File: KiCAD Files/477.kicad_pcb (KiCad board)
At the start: 2 copper layers, 101.7 x 59.6 mm, 74 parts, among them IC1 W25N01GVSFIG, IC2 W25N01GVSFIG, IC3 W25N01GVSFIG, IC4 W25N01GVSFIG, IC5 AZ1117IH-3.3TRG1, IC6 USBLC6-2SC6, J1 BM06B-SRSS-TBT_LF__SN_, J2 6364372-2, J3 TSW-103-14-S-D, J4 TSW-103-14-S-D, J5 BM07B-SRSS-TB_LF__SN_, J6 BM09B-SRSS-TB_LF__SN_, J7 TSW-105-05-F-S, U1 STM32H7A3RGTx, Y1 ABM8G-48.000MHZ-18-D2Y-T

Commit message: fixed weird routing
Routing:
- net VBAT: track 417.9 -> 404.6 mm
- net +5V: track 175.4 -> 163.6 mm

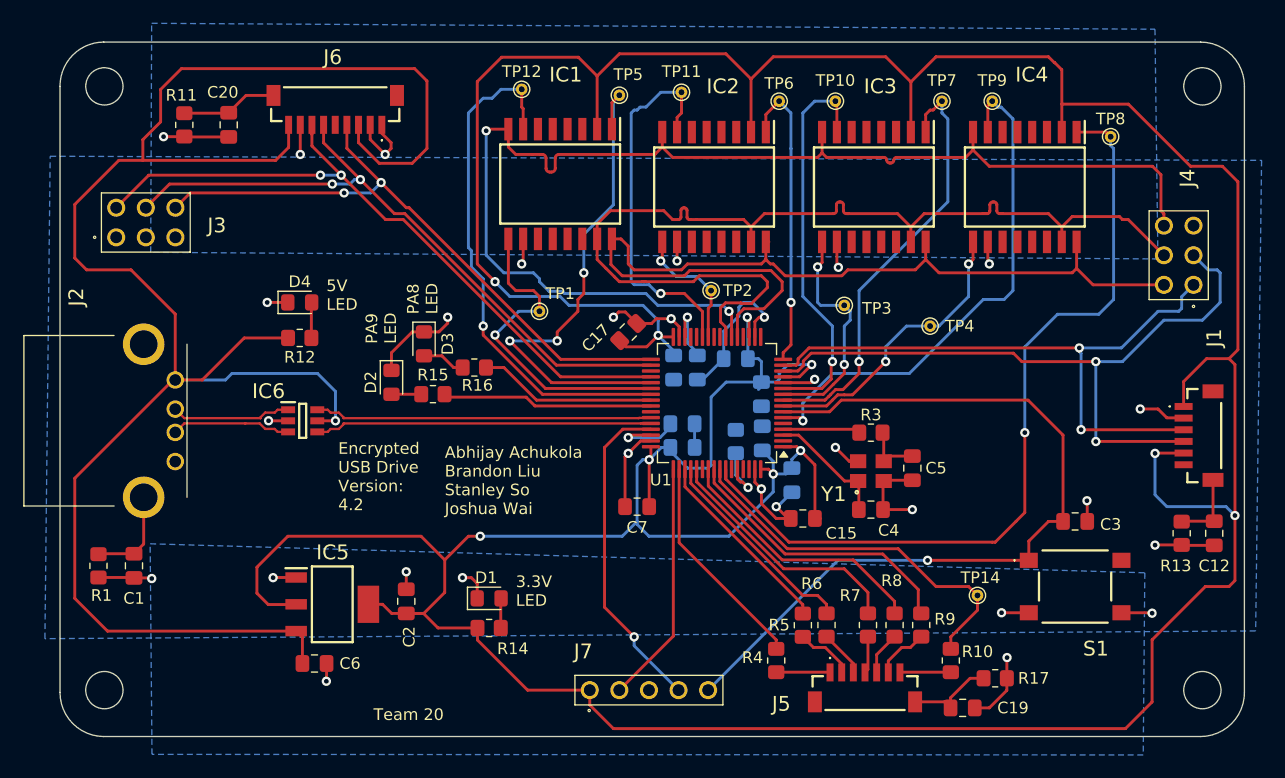
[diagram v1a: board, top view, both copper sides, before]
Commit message: made VBAT pad bigger
hi Joshua
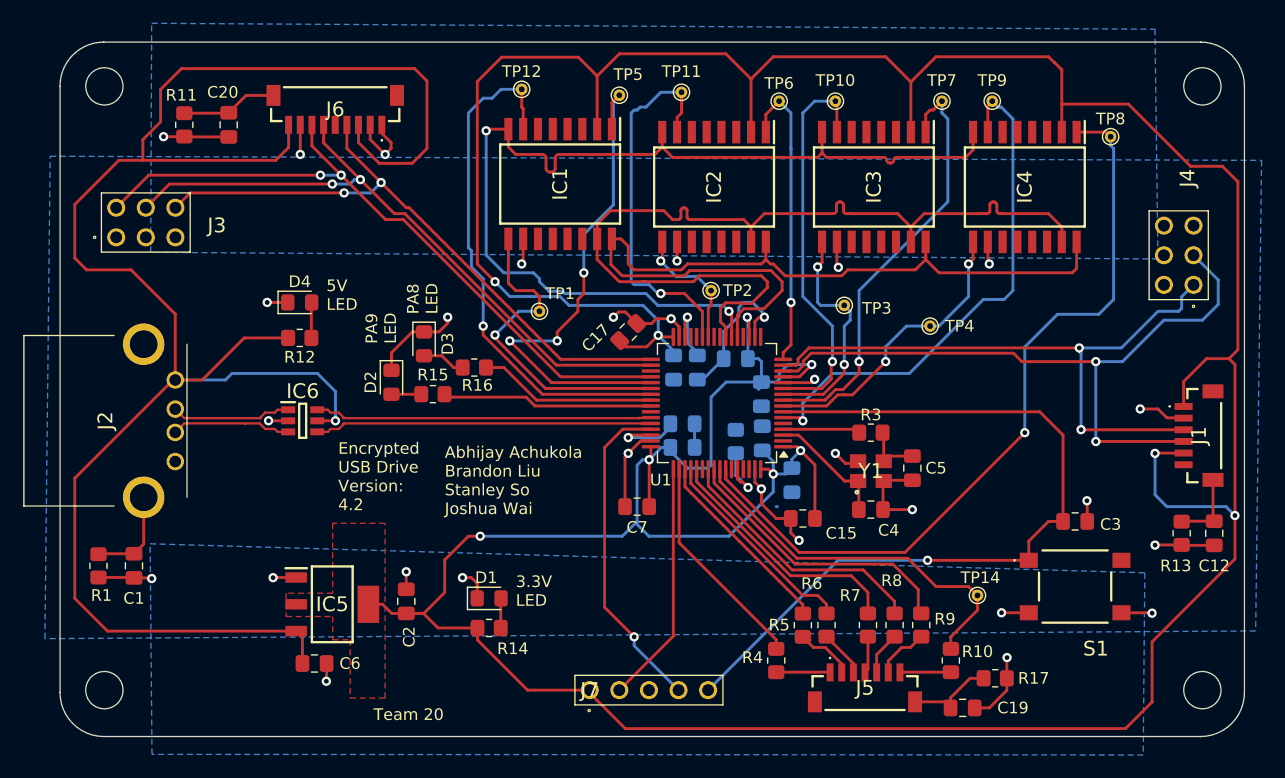
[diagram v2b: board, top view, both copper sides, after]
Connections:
- J4 pad 2: PA5/SCK -> unconnected-(J4-Pad2)
- J4 pad 4: PA7/MOSI -> unconnected-(J4-Pad4)
- J4 pad 6: PA6/MISO -> unconnected-(J4-Pad6)
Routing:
- net VBAT: track 404.6 -> 378.8 mm
- net PA6/MISO: track 109.8 -> 88.3 mm
- net PA7/MOSI: track 88.7 -> 78.2 mm
- net PA5/SCK: track 83.6 -> 74.8 mm
- net PB6/HOLD4: track 70.5 -> 67.2 mm
- net GND: track 120.9 -> 120.1 mm
- net nRST: track 71.3 -> 70.5 mm
- net unconnected-(J4-Pad2): track 0.00 -> 0.70 mm
- net PA0/FP TX: track 60.6 -> 60.0 mm
- added copper zone on F.Cu, net VBAT

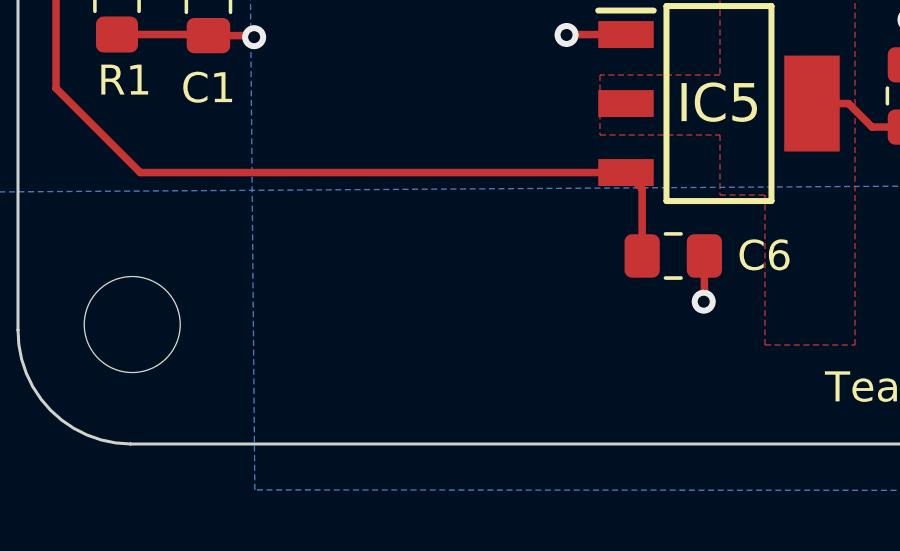
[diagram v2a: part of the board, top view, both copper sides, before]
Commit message: added big ground pad that we can clip oscilloscope to
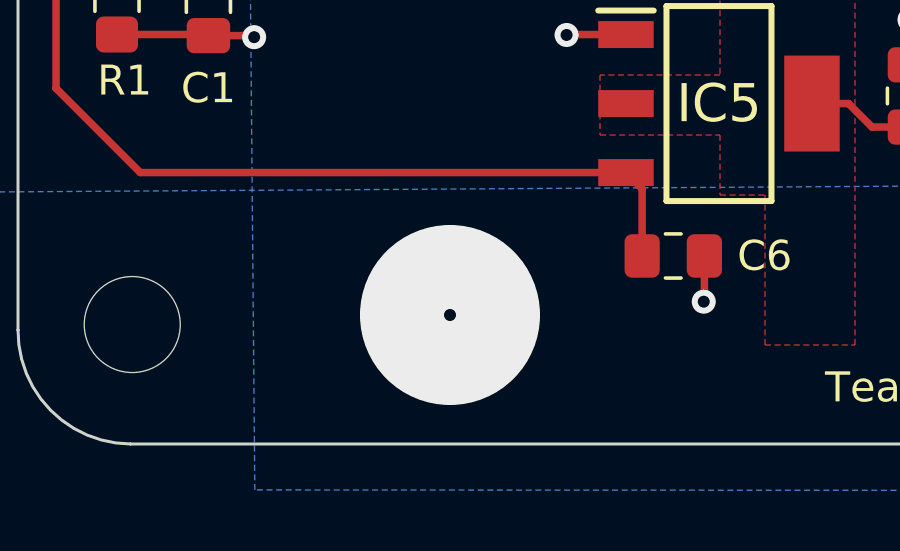
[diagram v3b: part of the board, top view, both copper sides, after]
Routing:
- net GND: vias 30 -> 31
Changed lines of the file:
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@@
+	)
+	(via
+		(at 100 131)
+		(size 6)
+		(drill 0.4)
+		(layers "F.Cu" "B.Cu")
+		(free yes)
+		(net 1)
 	)
 	(via

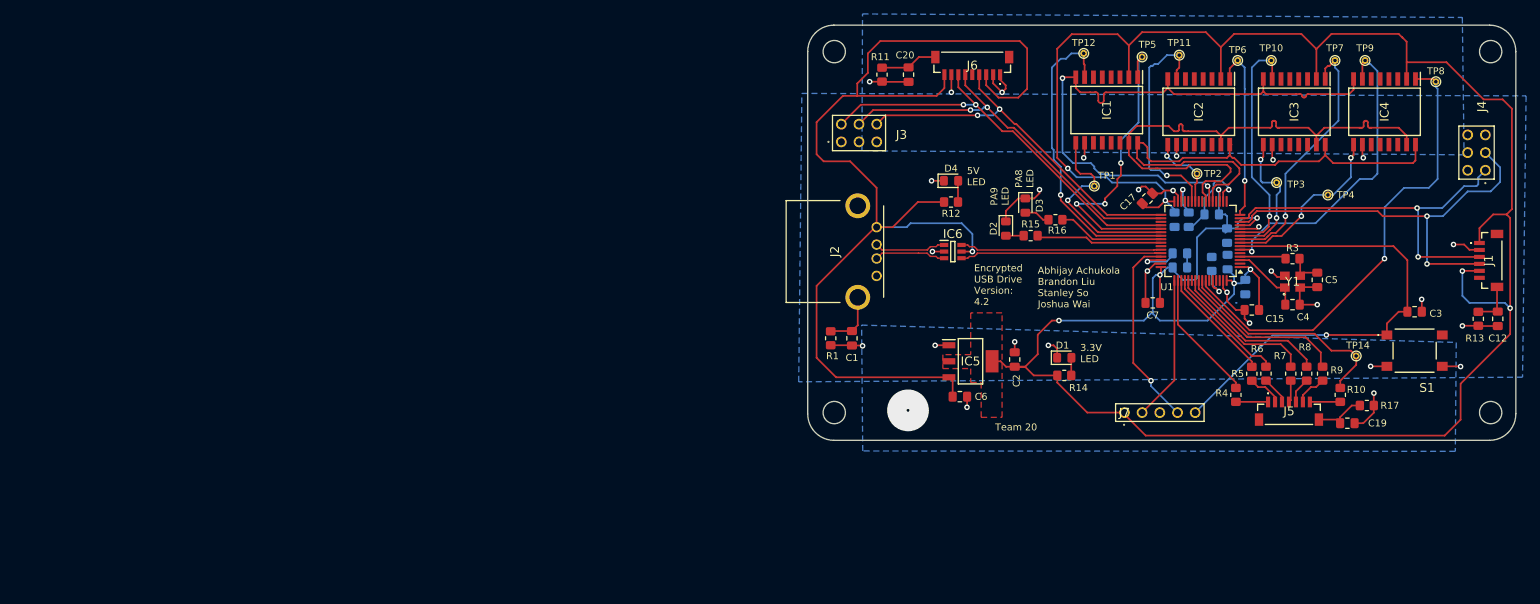
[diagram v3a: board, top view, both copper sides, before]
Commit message: added esd changes to schematic and pcb, mainly for J1 and J5, no DRC run
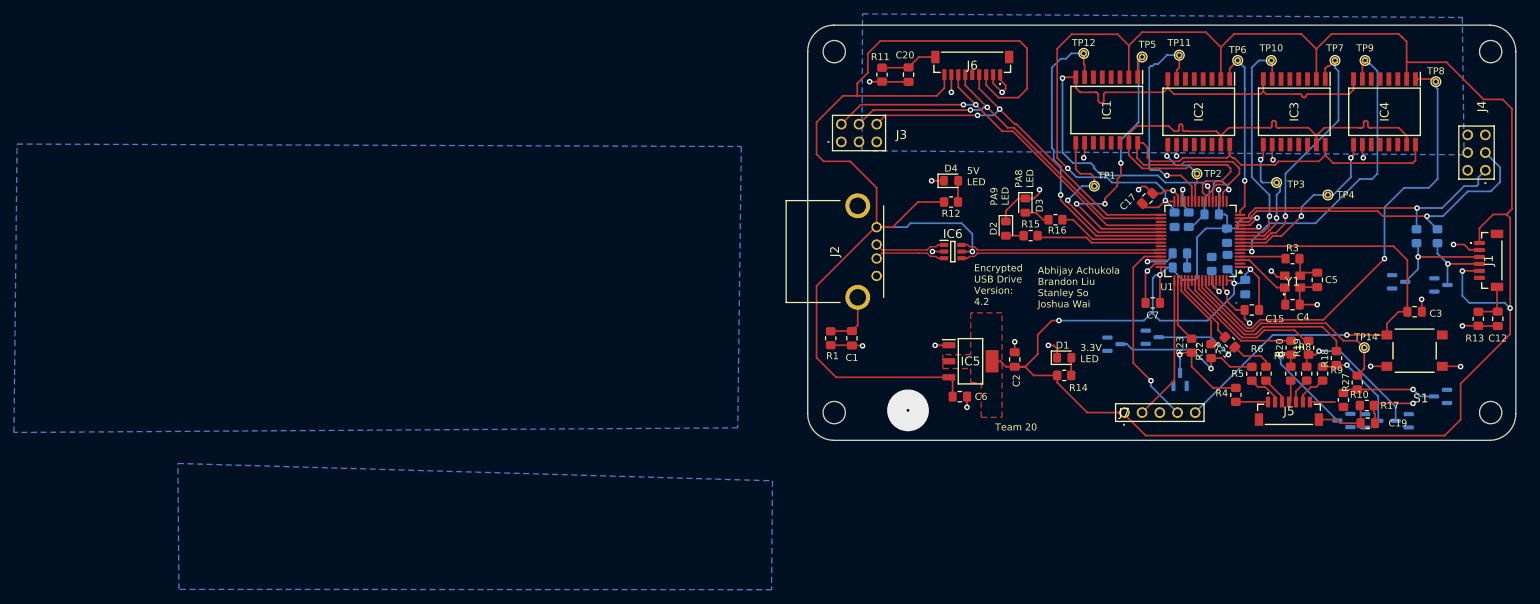
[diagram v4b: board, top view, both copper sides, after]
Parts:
- added D10: BZX84Cxx, Package_TO_SOT_SMD:SOT-23, B.Cu at (129.6, 121.5)
- added D11: BZX84Cxx, Package_TO_SOT_SMD:SOT-23, B.Cu at (139.1, 126.6)
- added D12: BZX84Cxx, Package_TO_SOT_SMD:SOT-23, B.Cu at (162.6, 132.4)
- added D13: BZX84Cxx, Package_TO_SOT_SMD:SOT-23, B.Cu at (166.6, 132.5)
- added D5: BZX84Cxx, Package_TO_SOT_SMD:SOT-23, B.Cu at (170.4, 112.5)
- added D6: BZX84Cxx, Package_TO_SOT_SMD:SOT-23, B.Cu at (176.5, 113.0)
- added D7: BZX84Cxx, Package_TO_SOT_SMD:SOT-23, B.Cu at (176.4, 129.0)
- added D8: BZX84Cxx, Package_TO_SOT_SMD:SOT-23, B.Cu at (170.9, 132.5)
- added D9: BZX84Cxx, Package_TO_SOT_SMD:SOT-23, B.Cu at (135.1, 120.5)
- added R18: 220, Resistor_SMD:R_0805_2012Metric_Pad1.20x1.40mm_HandSolder, F.Cu at (161.5, 123.5)
- added R19: 220, Resistor_SMD:R_0805_2012Metric_Pad1.20x1.40mm_HandSolder, F.Cu at (157.5, 122.0)
- added R20: 220, Resistor_SMD:R_0805_2012Metric_Pad1.20x1.40mm_HandSolder, F.Cu at (155.0, 122.0)
- added R21: 220, Resistor_SMD:R_0805_2012Metric_Pad1.20x1.40mm_HandSolder, F.Cu at (146.2, 121.2)
- added R22: 220, Resistor_SMD:R_0805_2012Metric_Pad1.20x1.40mm_HandSolder, F.Cu at (143.5, 122.5)
- added R23: 220, Resistor_SMD:R_0805_2012Metric_Pad1.20x1.40mm_HandSolder, F.Cu at (140.7, 121.7)
- added R24: 220, Resistor_SMD:R_0805_2012Metric_Pad1.20x1.40mm_HandSolder, B.Cu at (176.0, 106.0)
- added R25: 220, Resistor_SMD:R_0805_2012Metric_Pad1.20x1.40mm_HandSolder, B.Cu at (173.0, 106.0)
- added R27: 220, Resistor_SMD:R_0805_2012Metric_Pad1.20x1.40mm_HandSolder, F.Cu at (164.5, 127.0)
- moved C19 2.93 mm to (166.0, 132.8)
- moved TP14 1.66 mm to (165.5, 122.0)
- moved R10 0.85 mm to (162.5, 129.5)
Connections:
- J1 pad 3: PA1/FP RX -> FP RX
- J1 pad 4: PA0/FP TX -> FP TX
- J4 pad 1: PA1/FP RX -> PA1/FP RX ESD
- J4 pad 3: PA0/FP TX -> PA0/FP TX ESD
- R10 pad 1: PB5/KeyC3 -> KeyC3
- R4 pad 2: PA15/KeyR1 -> KeyR1
- R5 pad 2: PC10/KeyR2 -> KeyR2
- R6 pad 2: PC11/KeyR3 -> KeyR3
- R7 pad 1: PC12/KeyR4 -> KeyR4
- R8 pad 1: PB3/KeyC1 -> KeyC1
- R9 pad 2: PB4/KeyC2 -> KeyC2
- TP14 pad 1: PB5/KeyC3 -> PB5/KeyC3 ESD
- U1 pad 14: PA0/FP TX -> PA0/FP TX ESD
- U1 pad 15: PA1/FP RX -> PA1/FP RX ESD
- U1 pad 50: PA15/KeyR1 -> PA15/KeyR1 ESD
- U1 pad 51: PC10/KeyR2 -> PC10/KeyR2 ESD
- U1 pad 52: PC11/KeyR3 -> PC11/KeyR3 ESD
- U1 pad 53: PC12/KeyR4 -> PC12/KeyR4 ESD
- U1 pad 55: PB3/KeyC1 -> PB3/KeyC1 ESD
- U1 pad 56: PB4/KeyC2 -> PB4/KeyC2 ESD
- U1 pad 57: PB5/KeyC3 -> PB5/KeyC3 ESD
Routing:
- net PA0/FP TX: track 60.0 -> 0.00 mm, vias 2 -> 0
- net PA1/FP RX: track 55.5 -> 0.00 mm, vias 2 -> 0
- net PA0/FP TX ESD: track 0.00 -> 48.1 mm, vias 0 -> 1
- net PA1/FP RX ESD: track 0.00 -> 43.0 mm, vias 0 -> 1
- net PB5/KeyC3 ESD: track 0.00 -> 33.2 mm
- net PB5/KeyC3: track 32.7 -> 0.00 mm
- net PB4/KeyC2 ESD: track 0.00 -> 26.4 mm
- net PB4/KeyC2: track 24.6 -> 0.00 mm
- net PB3/KeyC1: track 22.6 -> 0.00 mm
- net KeyR2: track 0.00 -> 22.3 mm, vias 0 -> 1
- net PC12/KeyR4: track 21.5 -> 0.00 mm
- net PB3/KeyC1 ESD: track 0.00 -> 21.1 mm
- net KeyC1: track 0.00 -> 19.1 mm, vias 0 -> 1
- net PC12/KeyR4 ESD: track 0.00 -> 19.0 mm
- net PA15/KeyR1: track 18.9 -> 0.00 mm
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
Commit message: Finished with changes to fix electric issues.
power lines need to be relooked at
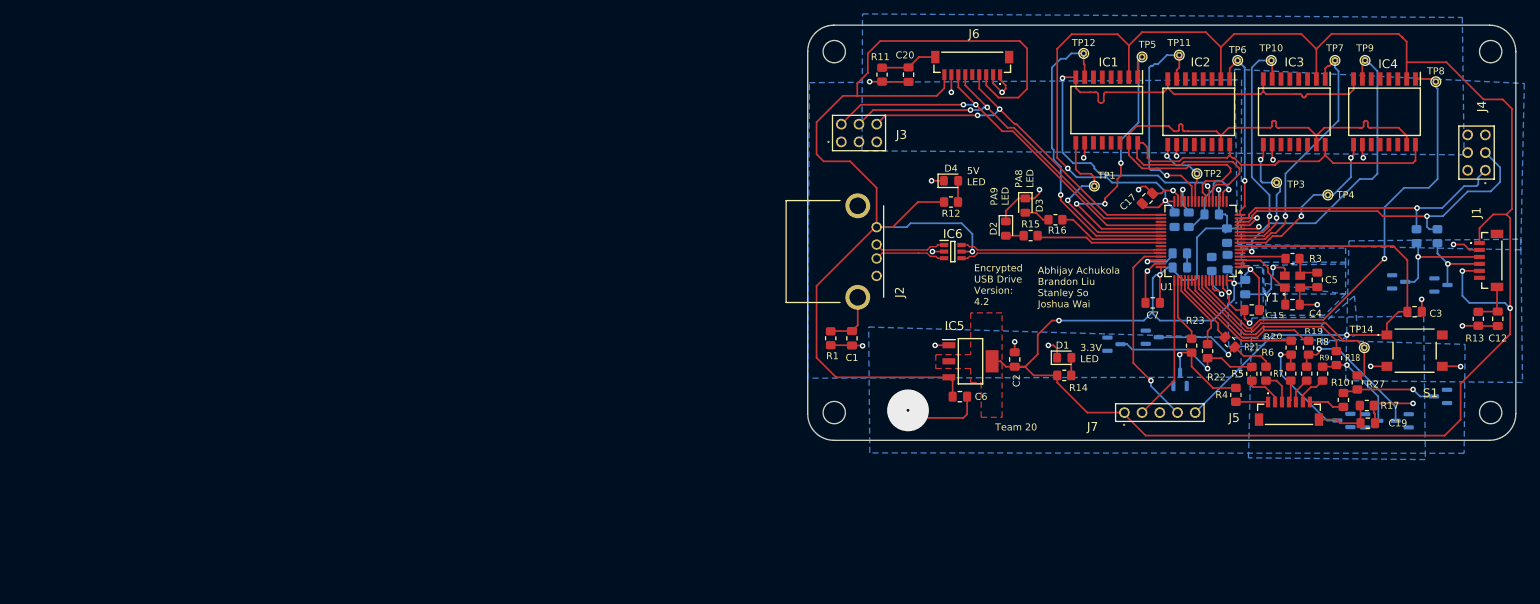
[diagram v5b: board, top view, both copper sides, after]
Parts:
- moved R22 0.50 mm to (143.0, 122.5)
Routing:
- net GND: track 122.2 -> 139.9 mm, vias 31 -> 30
- net Net-(J5-Pad7): track 3.64 -> 5.13 mm
- net /Microcontroller Circuitry/BOOT0: track 5.44 -> 6.69 mm
- net Net-(J5-Pad3): track 4.02 -> 4.90 mm
- net KeyR4: track 16.1 -> 16.9 mm
- net FP RX: track 15.2 -> 16.0 mm
- net PA0/FP TX ESD: track 48.1 -> 48.8 mm
- net KeyC1: track 19.1 -> 19.6 mm

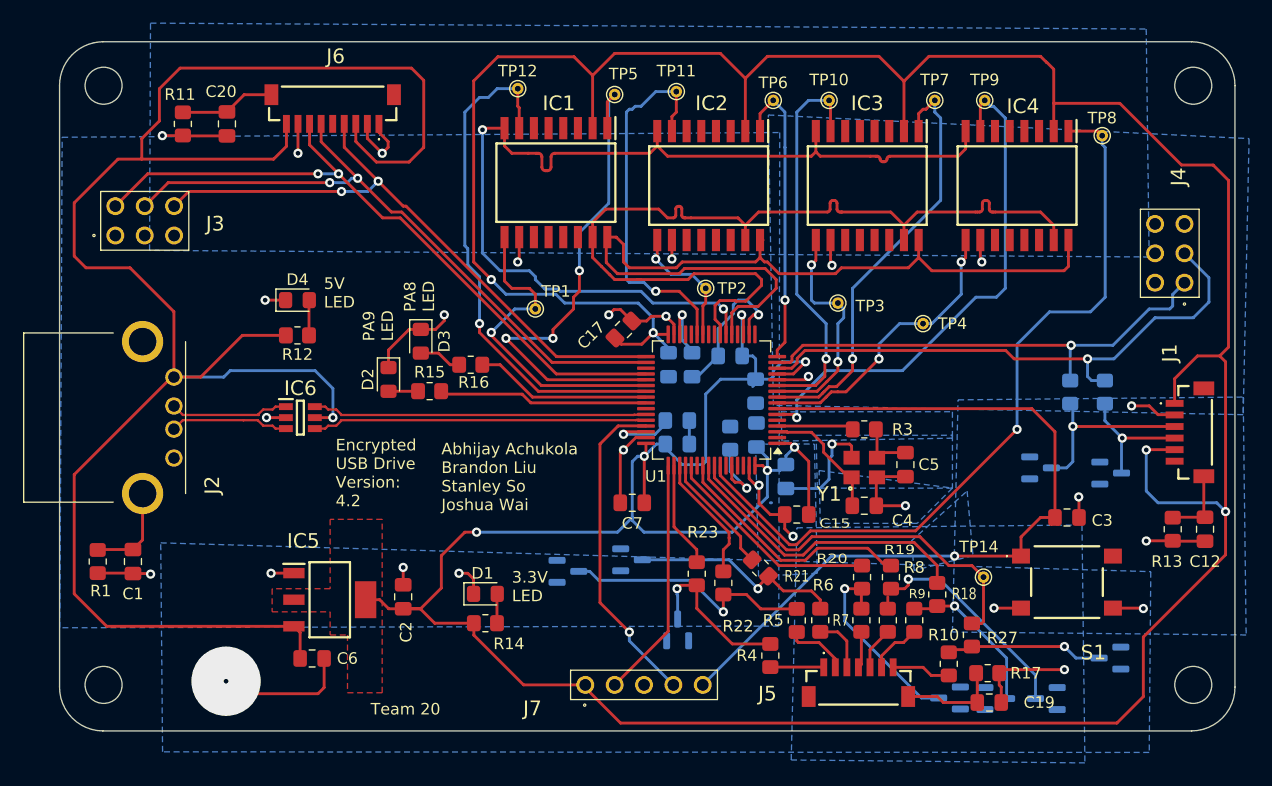
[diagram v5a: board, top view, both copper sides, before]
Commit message: rerouted keypad
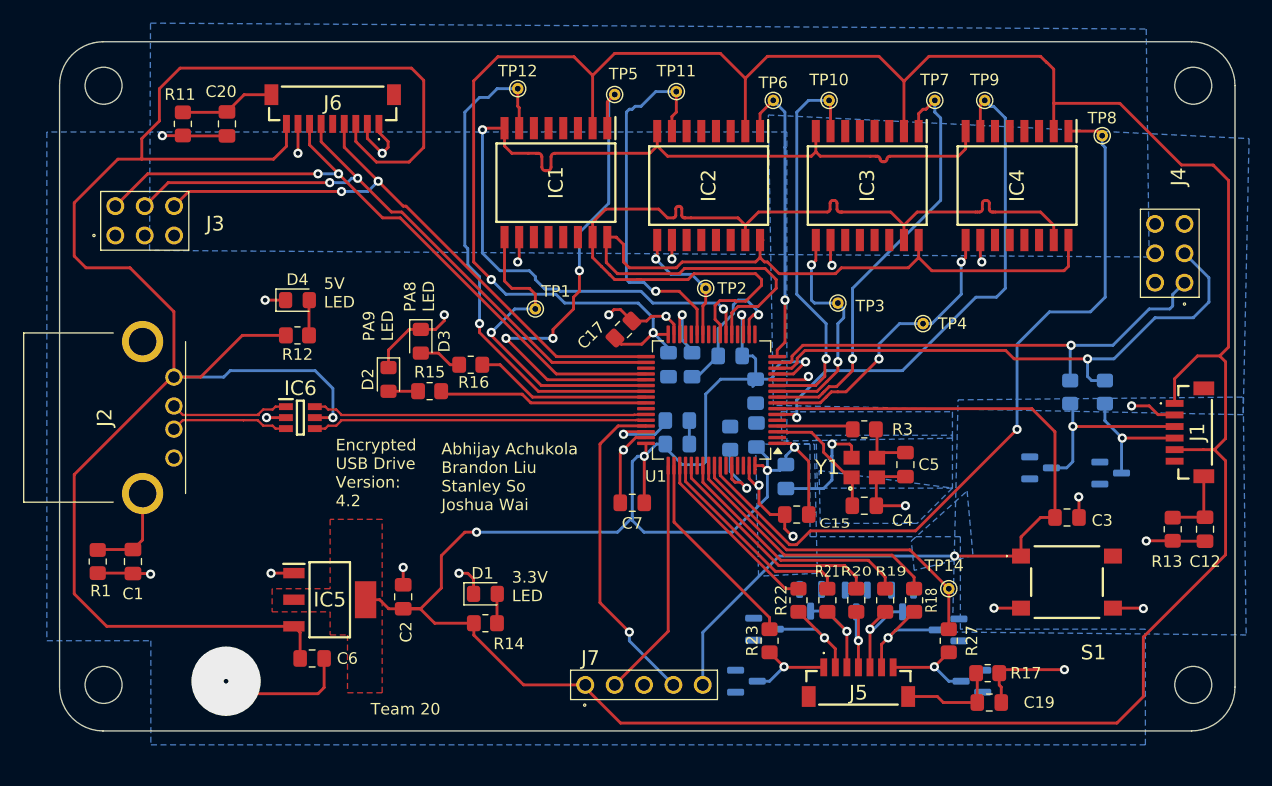
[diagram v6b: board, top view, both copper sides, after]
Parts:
- removed R10, R4, R5, R6, R7, R8, R9: 1k, Resistor_SMD:R_0805_2012Metric_Pad1.20x1.40mm_HandSolder
- R18, R19, R20, R21, R22, R23, R27: value 220 -> 1000
- moved D10 17.7 mm to (146.6, 126.5)
- moved D9 15.9 mm to (150.6, 124.0), turned to -90 degrees
- moved D8 15.0 mm to (158.5, 124.1), turned to -90 degrees
- moved D7 12.1 mm to (164.5, 131.0)
- moved D12 11.6 mm to (154.5, 124.1), turned to -90 degrees
- moved R23 8.55 mm to (147.0, 127.5)
- moved D11 7.42 mm to (145.0, 131.0), turned to 0 degrees
- moved D13 7.23 mm to (162.4, 126.6), turned to 180 degrees
- moved R22 6.67 mm to (149.5, 124.0)
- moved R21 6.43 mm to (152.0, 124.0), turned to 90 degrees
- moved TP14 3.16 mm to (162.5, 123.0)
- moved R18 2.06 mm to (159.5, 124.0)
- moved R19 2.06 mm to (157.0, 124.0)
- moved R20 2.06 mm to (154.5, 124.0)
- moved R27 2.06 mm to (162.5, 127.5)
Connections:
- J5 pad 1: Net-(J5-Pad1) -> KeyR1
- J5 pad 2: Net-(J5-Pad2) -> KeyR2
- J5 pad 3: Net-(J5-Pad3) -> KeyR3
- J5 pad 4: Net-(J5-Pad4) -> KeyR4
- J5 pad 5: Net-(J5-Pad5) -> KeyC1
- J5 pad 6: Net-(J5-Pad6) -> KeyC2
- J5 pad 7: Net-(J5-Pad7) -> KeyC3
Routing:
- net KeyR2: track 22.3 -> 10.7 mm
- net KeyC1: track 19.6 -> 8.78 mm
- net KeyR4: track 16.9 -> 7.45 mm
- net VBAT: track 379.2 -> 369.8 mm, vias 10 -> 8
- net KeyR3: track 18.6 -> 9.36 mm
- net PA15/KeyR1 ESD: track 9.17 -> 17.6 mm
- net PC11/KeyR3 ESD: track 10.5 -> 18.1 mm
- net KeyR1: track 14.1 -> 8.08 mm
- net Net-(J5-Pad2): track 5.47 -> 0.00 mm
- net KeyC3: track 13.6 -> 8.18 mm
- net Net-(J5-Pad7): track 5.13 -> 0.00 mm
- net PB5/KeyC3 ESD: track 33.7 -> 28.8 mm
- net Net-(J5-Pad3): track 4.90 -> 0.00 mm
- net Net-(J5-Pad6): track 4.68 -> 0.00 mm
- net Net-(J5-Pad1): track 4.63 -> 0.00 mm
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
